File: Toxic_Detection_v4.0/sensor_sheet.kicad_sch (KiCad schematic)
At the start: 17 parts, among them IC5 ADS7828E_2K5, IC6 ADS7828E_2K5, IC7 ADS7828E_2K5, J5 79107-7205, J6 79107-7205, Q1 BSS138-G, Q2 BSS138-G

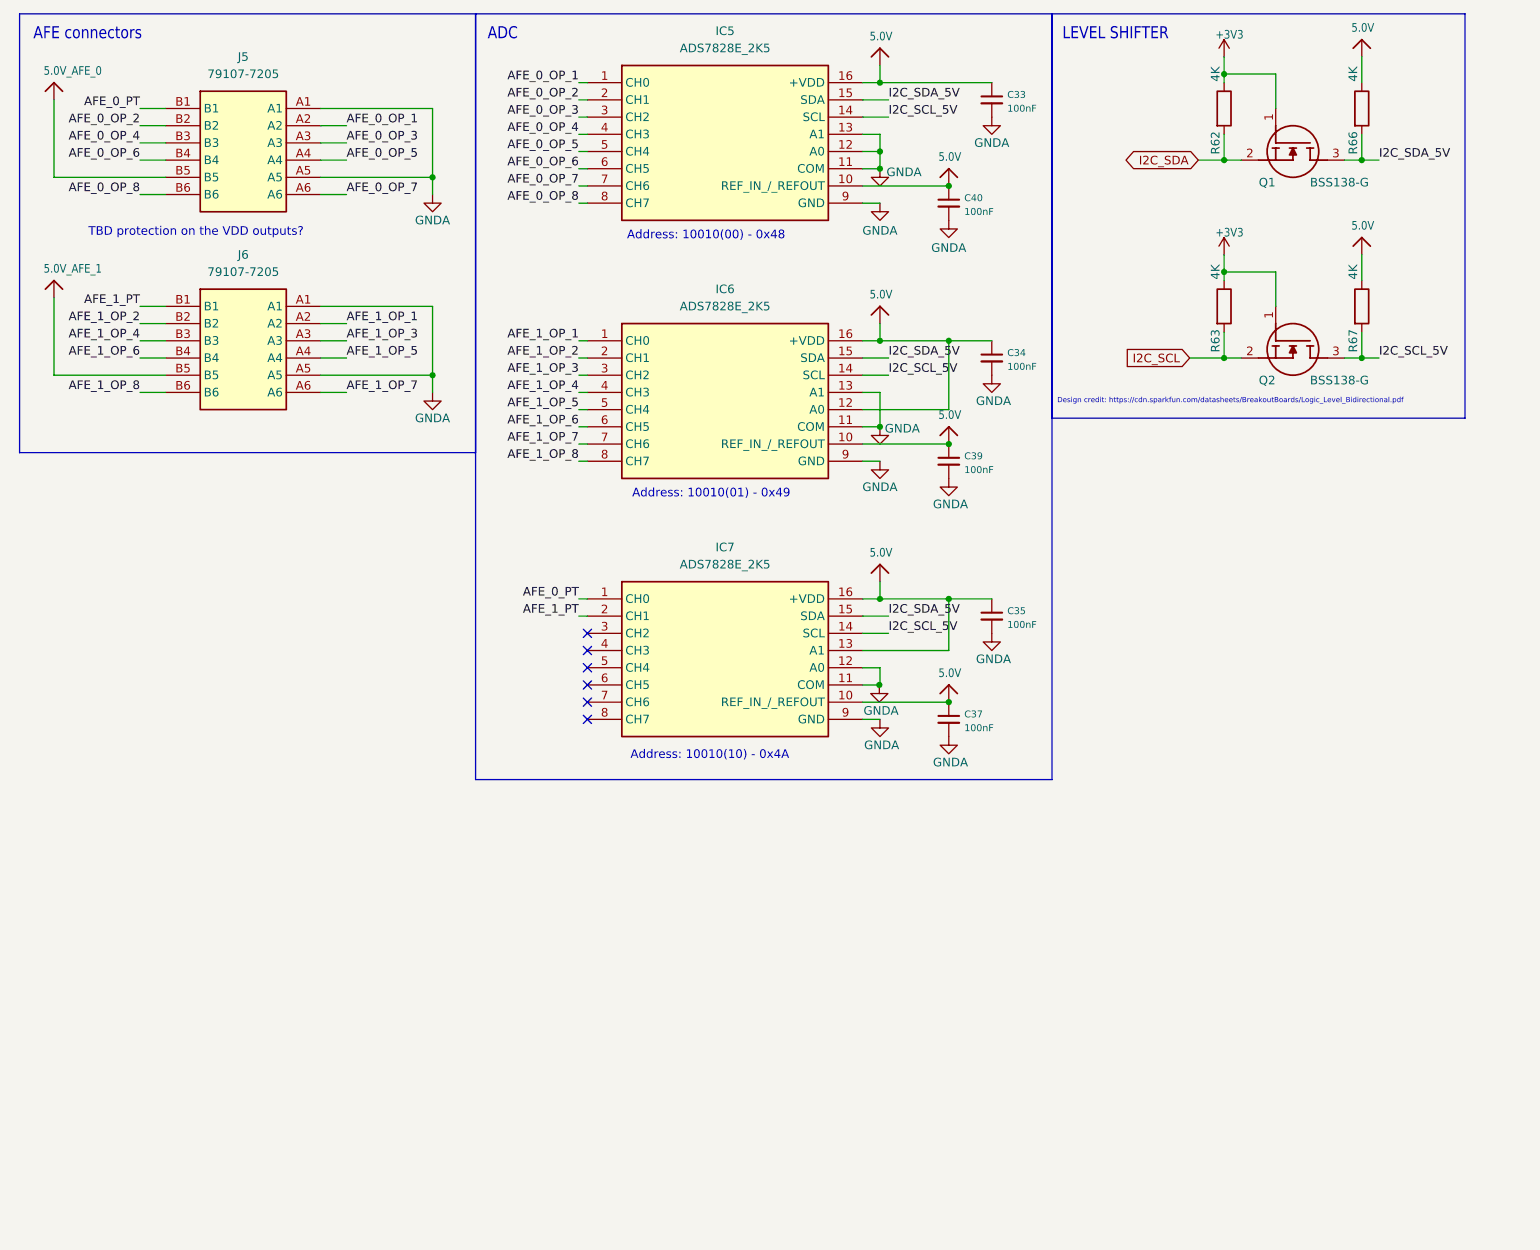
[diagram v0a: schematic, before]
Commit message: feat: add leds and headers
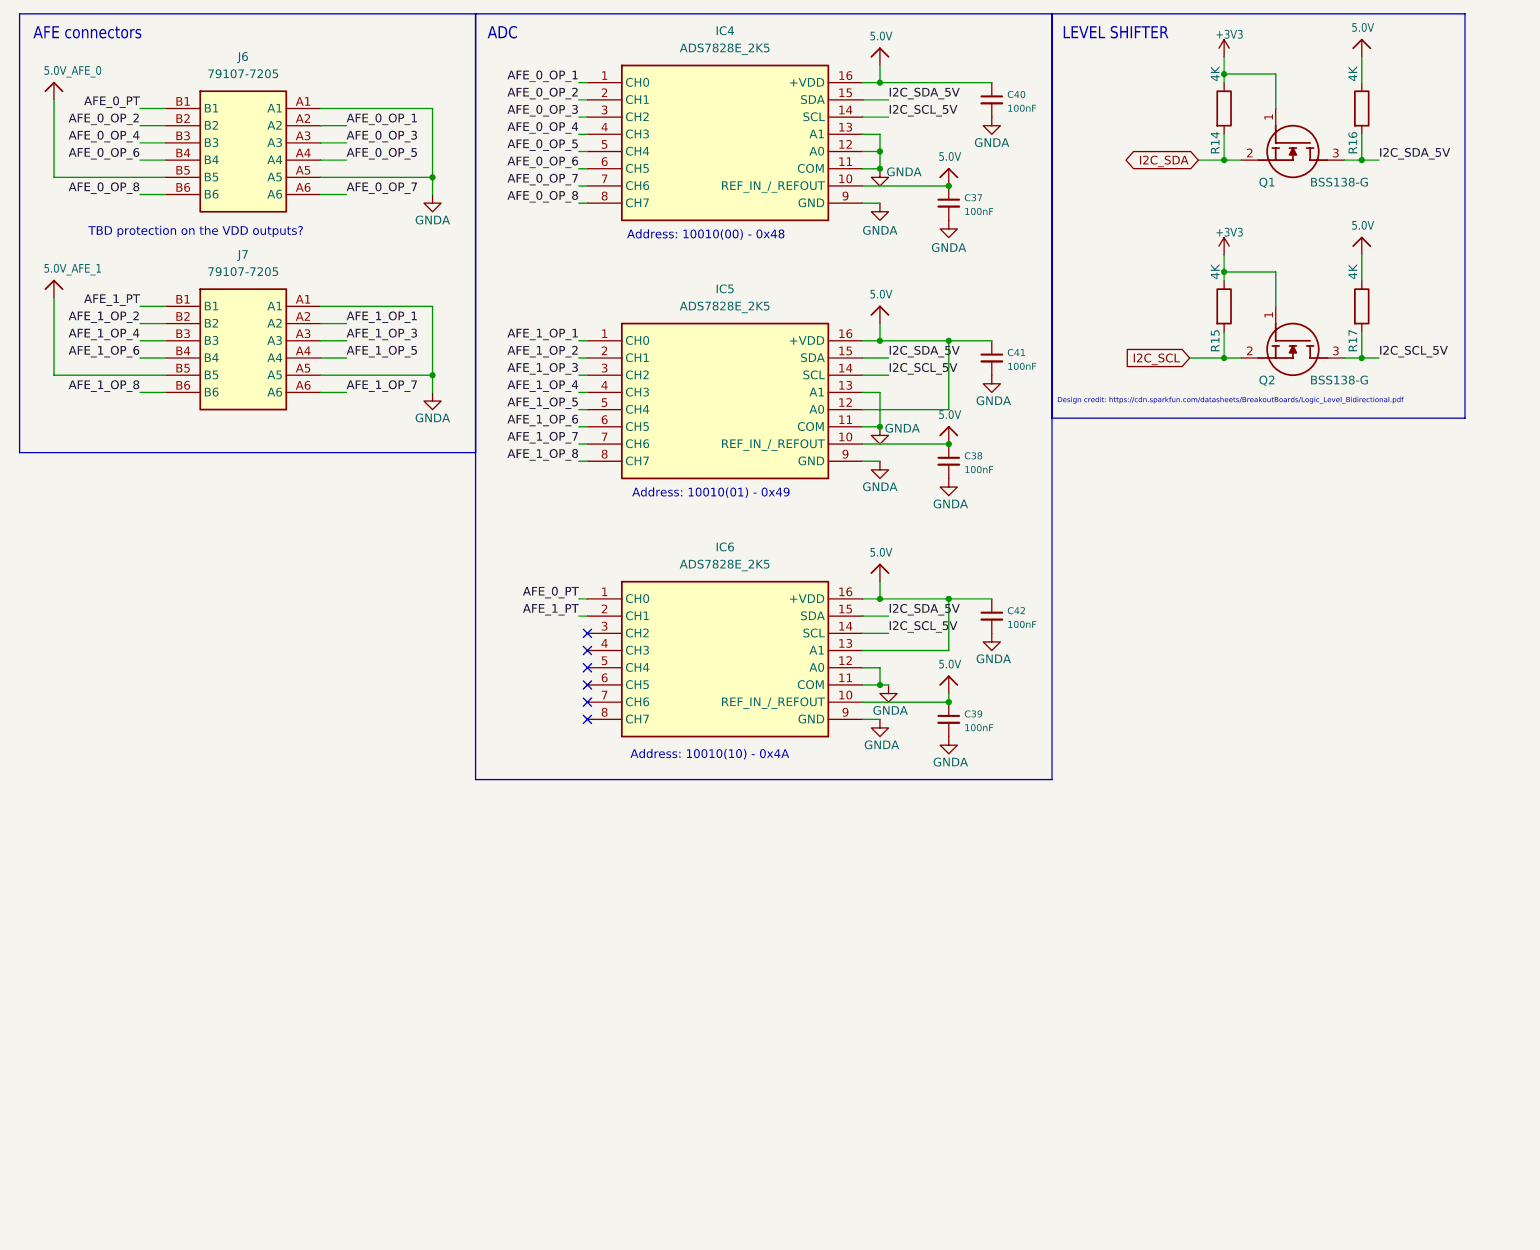
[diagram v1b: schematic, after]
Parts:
- renumbered C40 to C37, C39 to C38, C37 to C39, C33 to C40, C34 to C41, C35 to C42, IC5 to IC4, IC6 to IC5, IC7 to IC6, J5 to J6, J6 to J7, R62 to R14, R63 to R15, R66 to R16, R67 to R17

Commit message: feat: assign footprints and pass ERC
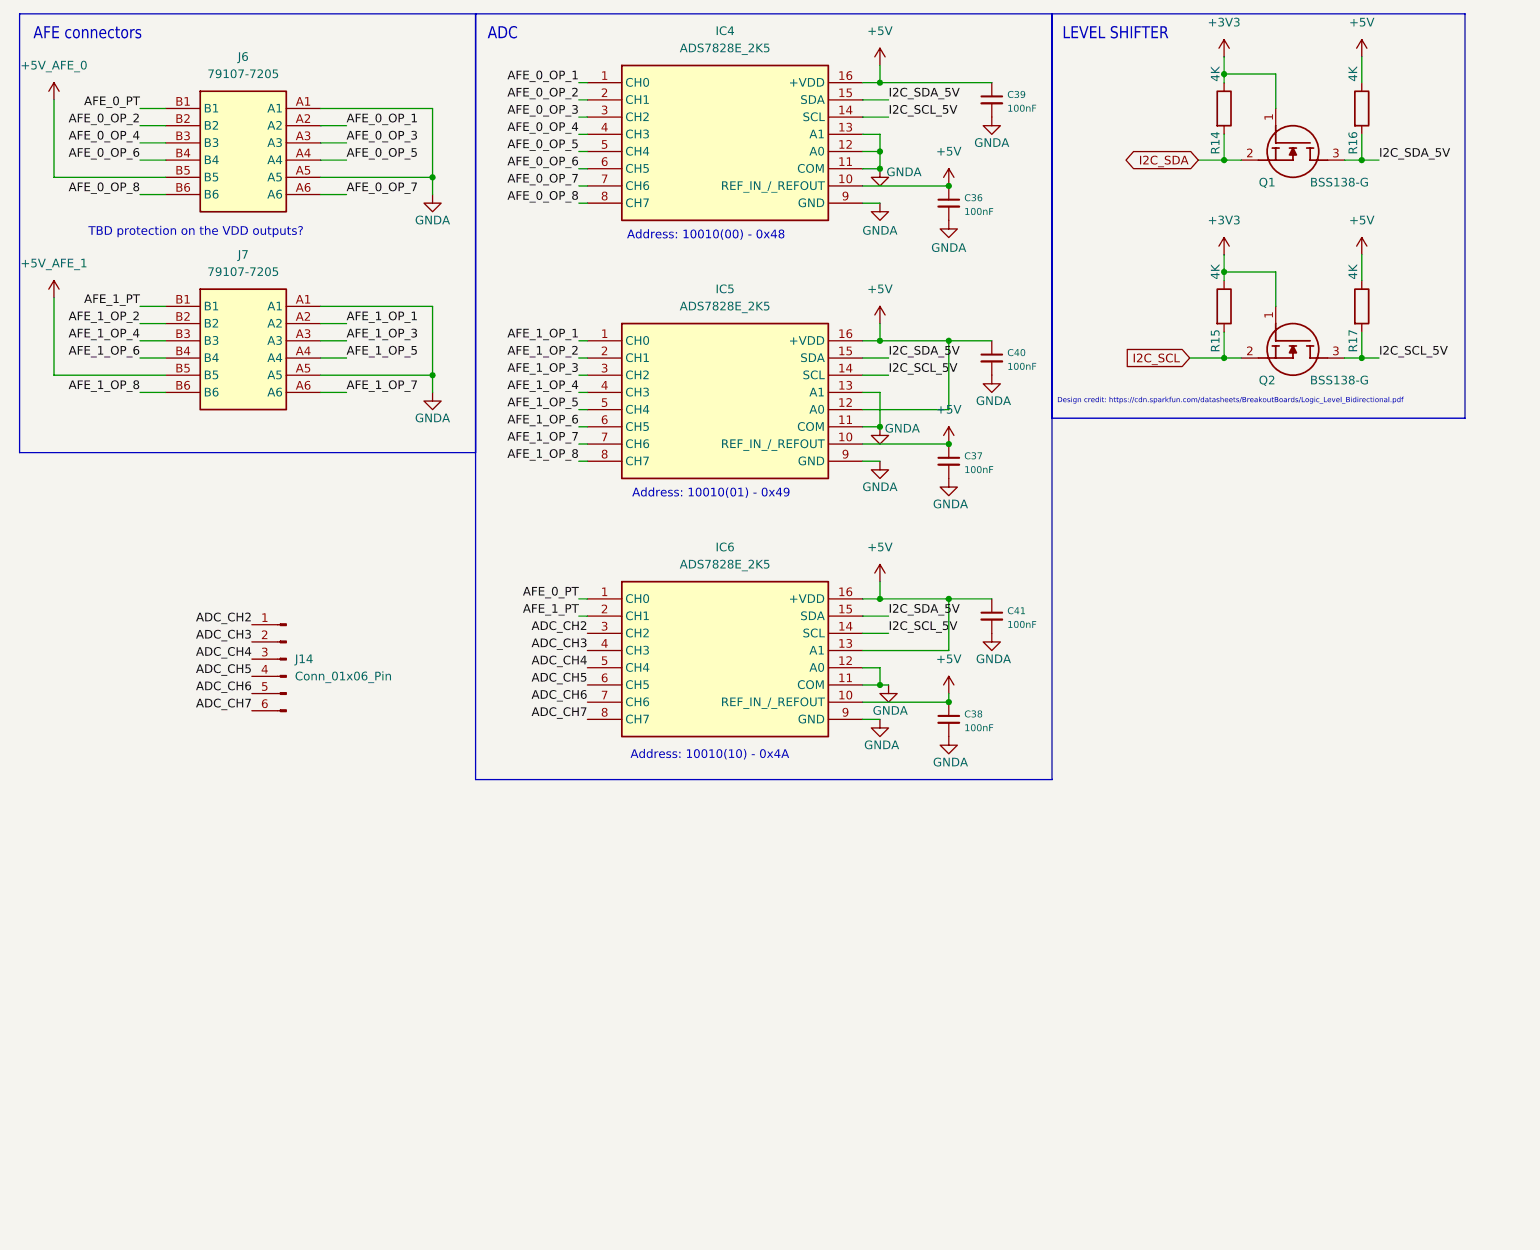
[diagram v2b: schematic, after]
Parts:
- added J14: Conn_01x06_Pin, Connector_PinSocket_2.54mm:PinSocket_1x06_P2.54mm_Vertical, symbol Connector:Conn_01x06_Pin
- C36: renamed from C37; footprint (none) -> Capacitor_SMD:C_0805_2012Metric_Pad1.18x1.45mm_HandSolder
- C37: renamed from C38; footprint (none) -> Capacitor_SMD:C_0805_2012Metric_Pad1.18x1.45mm_HandSolder
- C38: renamed from C39; footprint (none) -> Capacitor_SMD:C_0805_2012Metric_Pad1.18x1.45mm_HandSolder
- C39: renamed from C40; footprint (none) -> Capacitor_SMD:C_0805_2012Metric_Pad1.18x1.45mm_HandSolder
- C40: renamed from C41; footprint (none) -> Capacitor_SMD:C_0805_2012Metric_Pad1.18x1.45mm_HandSolder
- C41: renamed from C42; footprint (none) -> Capacitor_SMD:C_0805_2012Metric_Pad1.18x1.45mm_HandSolder
- IC4, IC5, IC6: footprint SOP65P640X120-16N -> ADC ADS7828:SOP65P640X120-16N
- J6, J7: footprint 791077205 -> AFE Connector 79107-7205:791077205
- Q1, Q2: footprint SOT96P237X111-3N -> NMOS-BSS138G:SOT96P237X111-3N
- R14, R15, R16, R17: footprint Resistor_SMD:R_0603_1608Metric -> Resistor_SMD:R_0805_2012Metric_Pad1.20x1.40mm_HandSolder
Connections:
- net ADC_CH2: now reaches IC6.3 (CH2)
- net ADC_CH2: now also J14.1 (Pin_1)
- net ADC_CH3: now reaches IC6.4 (CH3)
- net ADC_CH3: now also J14.2 (Pin_2)
- net ADC_CH4: now reaches IC6.5 (CH4)
- net ADC_CH4: now also J14.3 (Pin_3)
- net ADC_CH5: now reaches IC6.6 (CH5)
- net ADC_CH5: now also J14.4 (Pin_4)
- net ADC_CH6: now reaches IC6.7 (CH6)
- net ADC_CH6: now also J14.5 (Pin_5)
- net ADC_CH7: now reaches IC6.8 (CH7)
- net ADC_CH7: now also J14.6 (Pin_6)
- net 5.0V renamed +5V
- net 5.0V_AFE_0 renamed +5V_AFE_0
- net 5.0V_AFE_1 renamed +5V_AFE_1
- no-connect marks 6 -> 0

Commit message: doc: update schematic documentation, design notes and all other kind of documentation. Add product_brief revision history
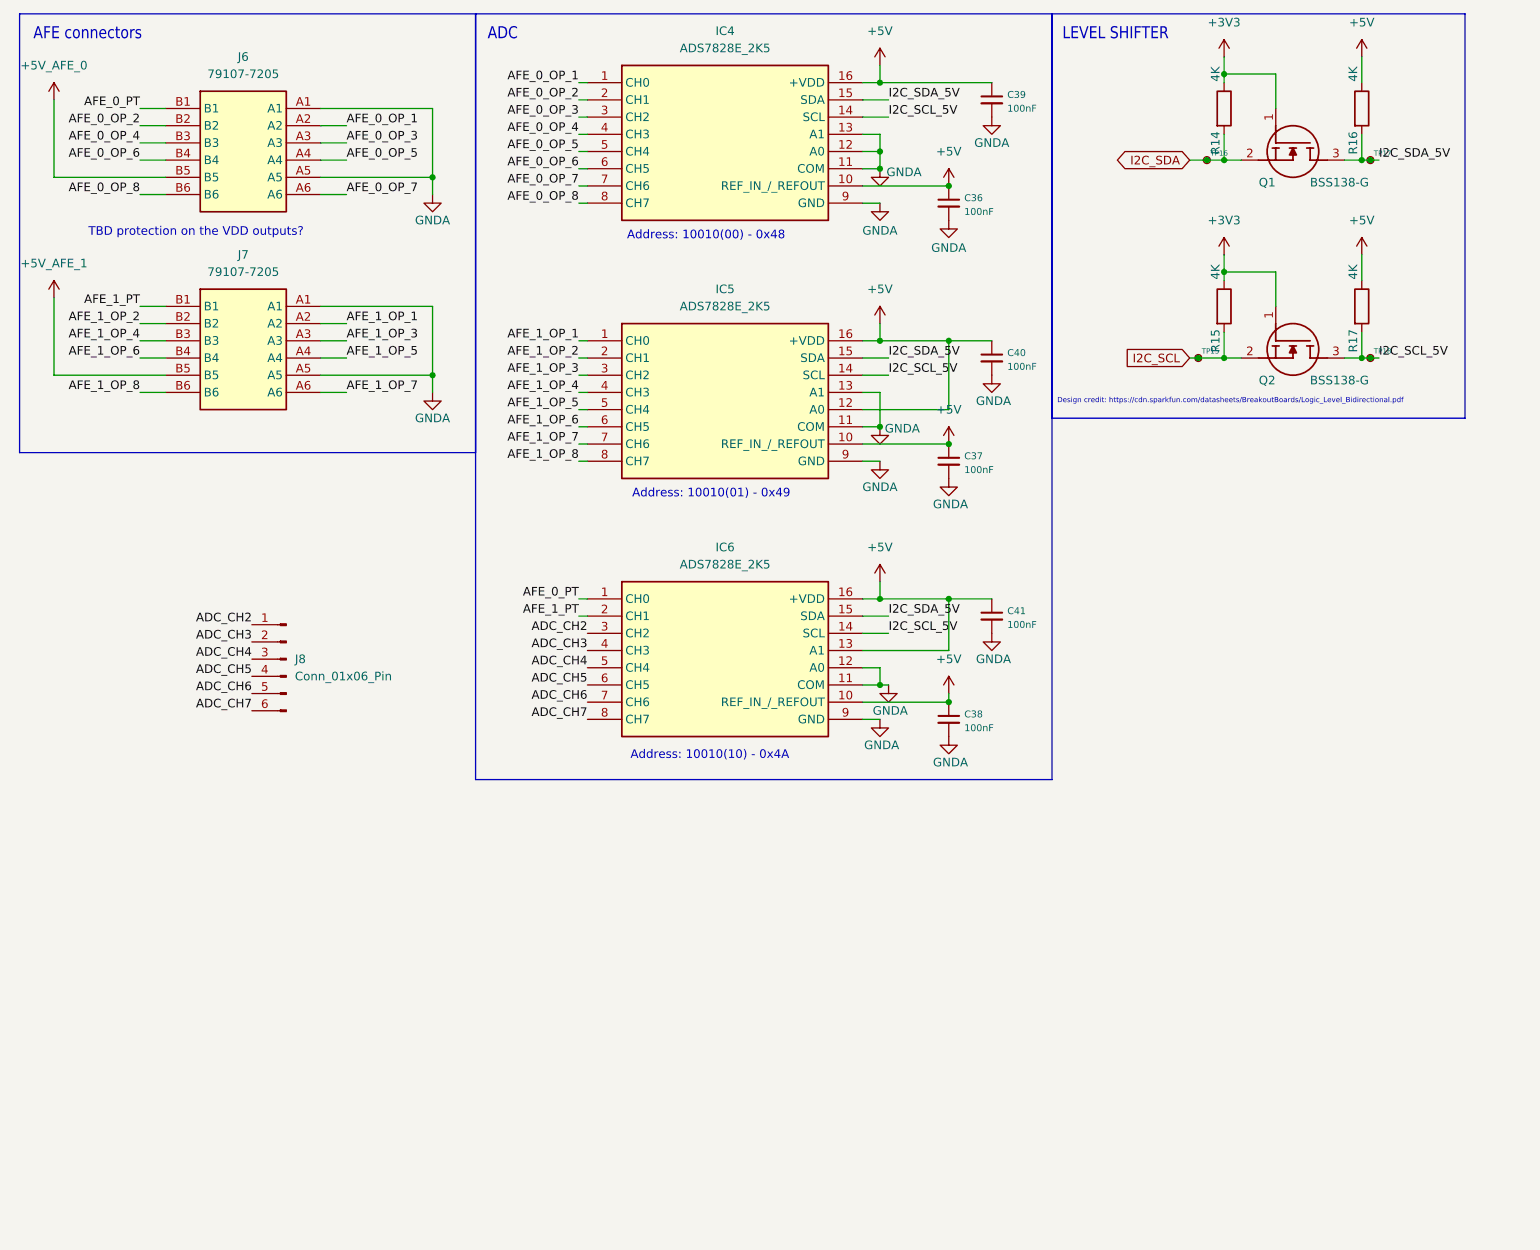
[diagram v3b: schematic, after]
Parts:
- added TP15, TP16, TP17, TP18: TestPoint_Small, TestPoint:TestPoint_Pad_D1.0mm, symbol Connector:TestPoint_Small
- renumbered J14 to J8
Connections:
- net I2C_SCL: now also TP15.1
- net I2C_SCL_5V: now also TP18.1
- net I2C_SDA: now also TP16.1
- net I2C_SDA_5V: now also TP17.1
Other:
- company: (none) -> Company: LNIS
- title: (none) -> Toxic_Detection_PCB

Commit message: feat: first placement (layout)
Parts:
- J8: footprint Connector_PinSocket_2.54mm:PinSocket_1x06_P2.54mm_Vertical -> Connector_PinHeader_2.54mm:PinHeader_2x03_P2.54mm_Vertical
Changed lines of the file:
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@@
 		(title "Toxic_Detection_PCB")
 		(date "2026-02-12")
-		(rev "4.0")
+		(rev "4.1")
 		(company "Company: LNIS")
 		(comment 4 "Author: Paul Capgras")
@@
 			)
 		)
-		(property "Footprint" "Connector_PinSocket_2.54mm:PinSocket_1x06_P2.54mm_Vertical"
+		(property "Footprint" "Connector_PinHeader_2.54mm:PinHeader_2x03_P2.54mm_Vertical"
 			(at 52.07 107.95 0)
 			(effects
